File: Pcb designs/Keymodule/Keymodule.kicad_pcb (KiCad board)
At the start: 2 copper layers, 105 parts, among them J1 USB connect, U1 RP2040, U2 SN74LV1T34DBV, U3 AMS1117-3.3, U4 W25Q128JVS, Y1 ABM8-272-T3

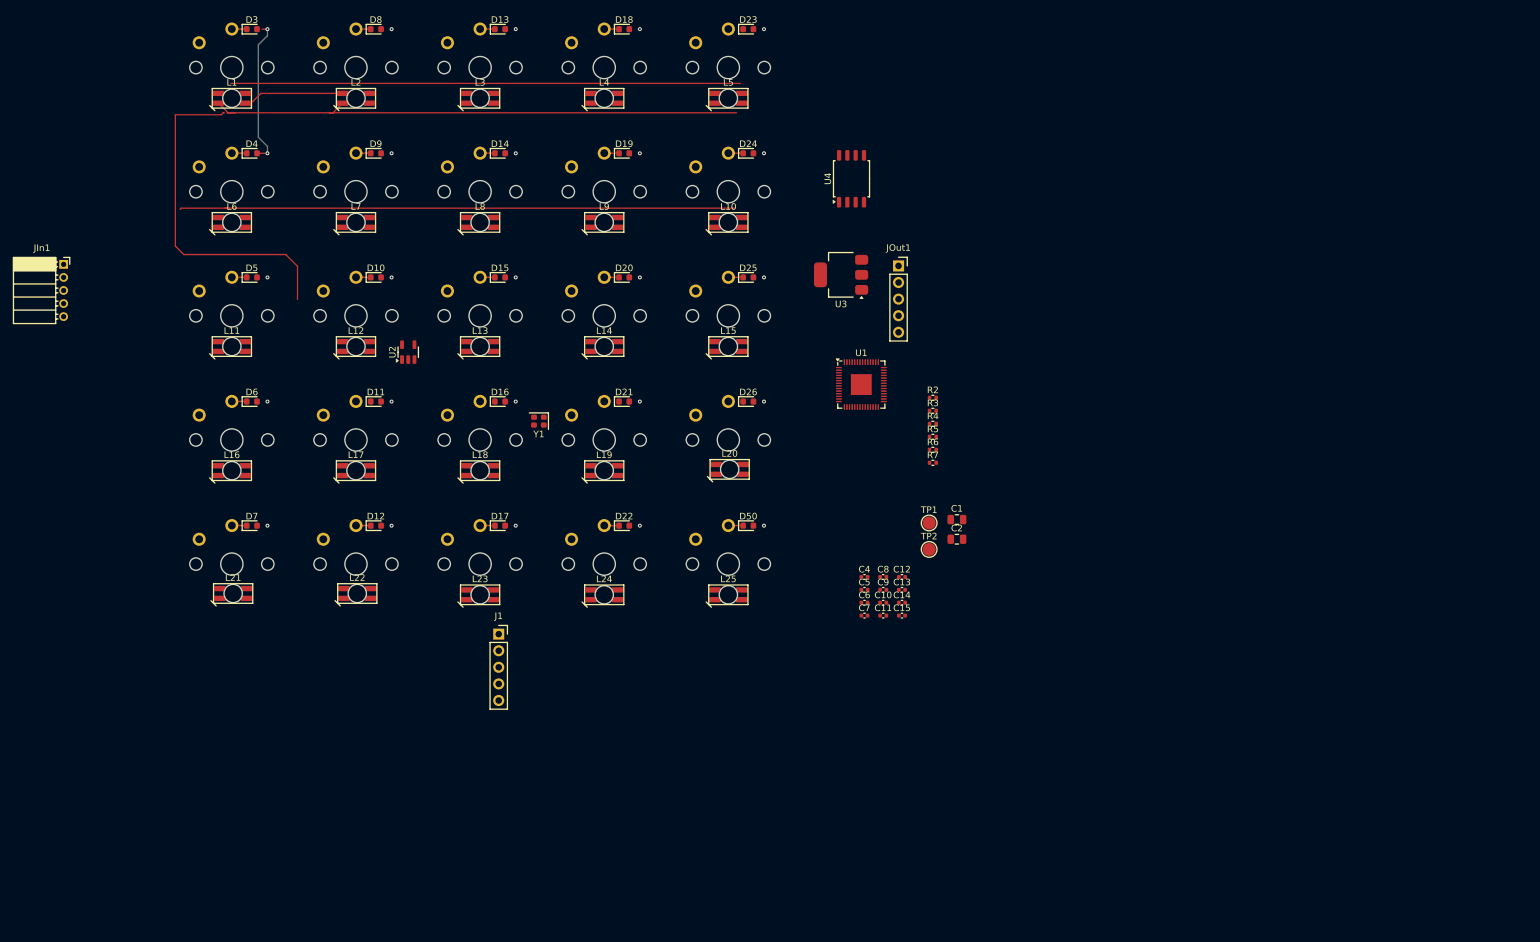
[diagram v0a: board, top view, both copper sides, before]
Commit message: Added traces to buttons
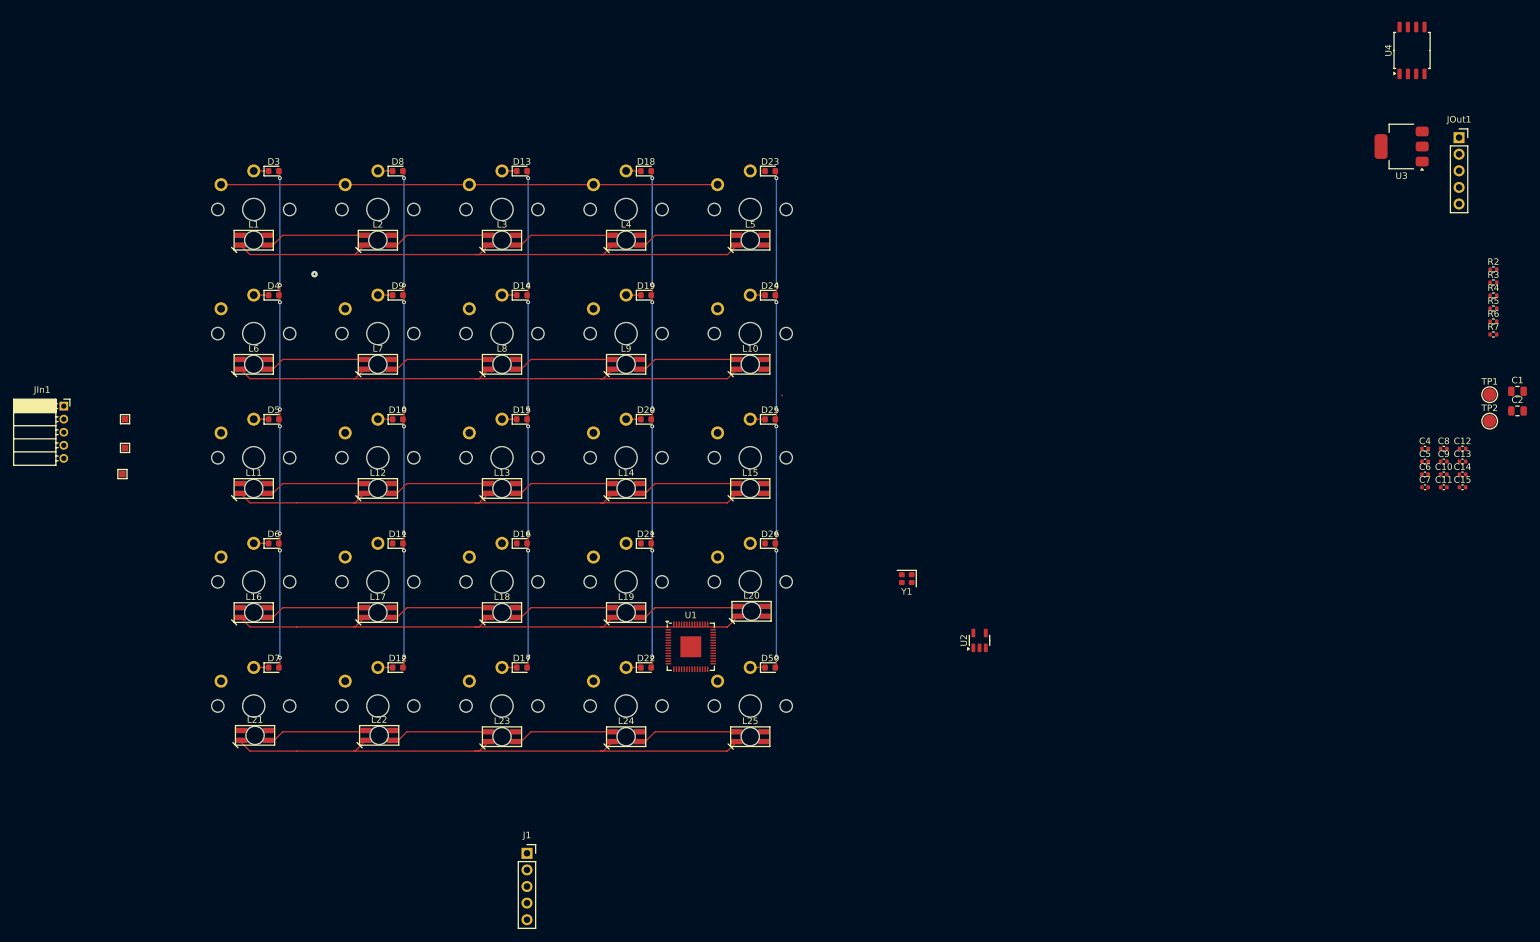
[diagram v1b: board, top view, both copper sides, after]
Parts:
- added REF**: TestPoint_Pad_1.0x1.0mm, TestPoint:TestPoint_Pad_1.0x1.0mm, F.Cu at (42.3, 94.1)
- added REF**: TestPoint_Pad_1.0x1.0mm, TestPoint:TestPoint_Pad_1.0x1.0mm, F.Cu at (41.9, 102.5)
- added REF**: TestPoint_Pad_1.0x1.0mm, TestPoint:TestPoint_Pad_1.0x1.0mm, F.Cu at (42.3, 98.5)
- moved U2 98.0 mm to (173.1, 128.0)
- moved C1 88.0 mm to (255.4, 89.8)
- moved C10 88.0 mm to (244.2, 102.6)
- moved C11 88.0 mm to (244.2, 104.5)
- moved C12 88.0 mm to (247.0, 98.6)
- moved C13 88.0 mm to (247.0, 100.6)
- moved C14 88.0 mm to (247.0, 102.6)
- moved C15 88.0 mm to (247.0, 104.5)
- moved C2 88.0 mm to (255.4, 92.8)
- moved C8 88.0 mm to (244.2, 98.6)
- moved C9 88.0 mm to (244.2, 100.6)
- moved JOut1 88.0 mm to (246.5, 51.0)
- moved TP1 88.0 mm to (251.2, 90.3)
- moved TP2 88.0 mm to (251.2, 94.4)
- moved U4 88.0 mm to (239.3, 37.7)
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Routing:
- net +5V: track 83.7 -> 422.9 mm
- net (no net): track 237.4 -> 0.14 mm, vias 25 -> 1
- net col0: track 0.00 -> 76.0 mm
- net row4: track 0.00 -> 75.3 mm, vias 0 -> 8
- net row3: track 0.00 -> 75.3 mm, vias 0 -> 8
- net row2: track 0.00 -> 75.3 mm, vias 0 -> 8
- net row1: track 0.00 -> 75.3 mm, vias 0 -> 8
- net row0: track 1.20 -> 75.6 mm, vias 0 -> 8
- net Net-(L4-DOUT): track 0.00 -> 15.5 mm
- net Net-(L24-DOUT): track 0.00 -> 15.5 mm
- net Net-(L19-DOUT): track 0.00 -> 15.5 mm
- net Net-(L14-DOUT): track 0.00 -> 15.5 mm
- net Net-(L10-DIN): track 0.00 -> 15.5 mm
- net Net-(L8-DOUT): track 0.00 -> 15.5 mm
- net Net-(L7-DOUT): track 0.00 -> 15.5 mm
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
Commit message: Stared wiring ic
LED signal boost not done
But its a start
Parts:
- added REF**: PinHeader_1x01_P1.27mm_Horizontal, Connector_PinHeader_1.27mm:PinHeader_1x01_P1.27mm_Horizontal, F.Cu at (139.9, 90.5)
- added REF**: PinHeader_1x01_P1.27mm_Horizontal, Connector_PinHeader_1.27mm:PinHeader_1x01_P1.27mm_Horizontal, F.Cu at (139.6, 109.5)
- added REF**: PinHeader_1x01_P1.27mm_Horizontal, Connector_PinHeader_1.27mm:PinHeader_1x01_P1.27mm_Horizontal, F.Cu at (60.5, 109.5)
- added REF**: PinHeader_1x01_P1.27mm_Horizontal, Connector_PinHeader_1.27mm:PinHeader_1x01_P1.27mm_Horizontal, F.Cu at (60.4, 90.5)
- added REF**: PinHeader_1x03_P1.27mm_Horizontal, Connector_PinHeader_1.27mm:PinHeader_1x03_P1.27mm_Horizontal, F.Cu at (50.9, 100.3)
- M_SW1, M_SW10, M_SW11, M_SW12, M_SW13, M_SW14, M_SW15, M_SW16, M_SW17, M_SW18, M_SW19, M_SW2, M_SW20, M_SW21, M_SW22, M_SW23, M_SW24, M_SW25, M_SW3, M_SW4, M_SW5, M_SW6, M_SW7, M_SW8, M_SW9: footprint 1_Custom_library:Kailh Switch 1350 -> 1_Custom_library:Kailh low profile Choc switch V1; moved to B.Cu
- moved C13 172.2 mm to (77.3, 71.7), turned to -90 degrees
- moved R5 169.7 mm to (82.1, 73.1), turned to 180 degrees
- moved C14 167.7 mm to (82.1, 72.0)
- moved U4 136.5 mm to (107.4, 72.6), turned to -90 degrees
- moved U2 132.0 mm to (56.0, 67.0), turned to -90 degrees
- moved R4 117.6 mm to (161.4, 150.4), turned to -90 degrees
- moved TP1 105.6 mm to (164.1, 150.0)
- moved C12 101.1 mm to (160.2, 150.4), turned to 90 degrees
- moved Y1 94.8 mm to (79.5, 71.7)
- moved C4 86.7 mm to (164.5, 138.9)
- moved C9 86.1 mm to (161.9, 126.2), turned to 90 degrees
- moved C10 82.5 mm to (174.2, 146.2)
- moved C11 82.5 mm to (174.2, 148.2)
- moved C15 82.5 mm to (177.1, 148.2)
- moved C5 82.5 mm to (171.3, 144.3)
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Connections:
- Y1 pad 4: GND -> unconnected-(Y1-Vdd-Pad4)
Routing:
- net GND: track 0.00 -> 694.7 mm
- net col4: track 0.00 -> 76.0 mm
- net col3: track 0.00 -> 76.0 mm
- net col2: track 0.00 -> 76.0 mm
- net +5V: track 422.9 -> 479.7 mm, vias 0 -> 2
- net col1: track 0.00 -> 38.0 mm
- net Net-(U1-GPIO15): track 0.00 -> 33.0 mm
- net row1: track 75.3 -> 44.2 mm, vias 8 -> 6
- net Net-(U1-QSPI_SD3): track 0.00 -> 20.4 mm
- net Net-(U1-QSPI_SCLK): track 0.00 -> 19.2 mm
- net col0: track 76.0 -> 57.0 mm
- net row2: track 75.3 -> 56.5 mm, vias 8 -> 6
- net Net-(U1-QSPI_SS): track 0.00 -> 18.3 mm
- net Net-(U1-QSPI_SD1): track 0.00 -> 17.1 mm
- net Net-(U1-QSPI_SD0): track 0.00 -> 16.8 mm
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
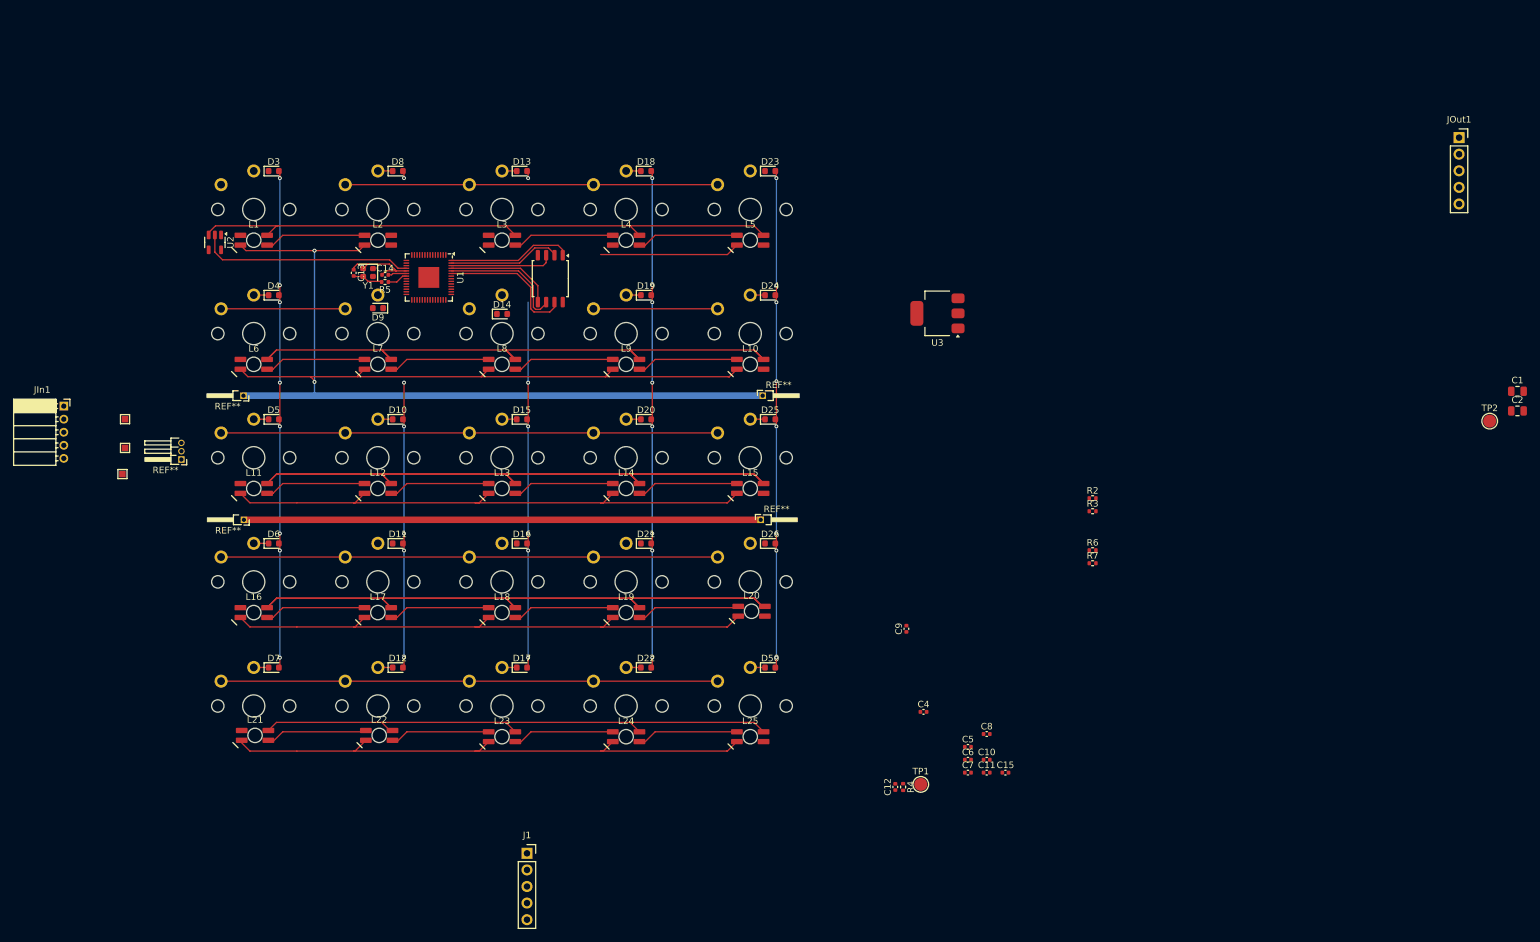
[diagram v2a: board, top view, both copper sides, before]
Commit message: Wired main power caps but to little space
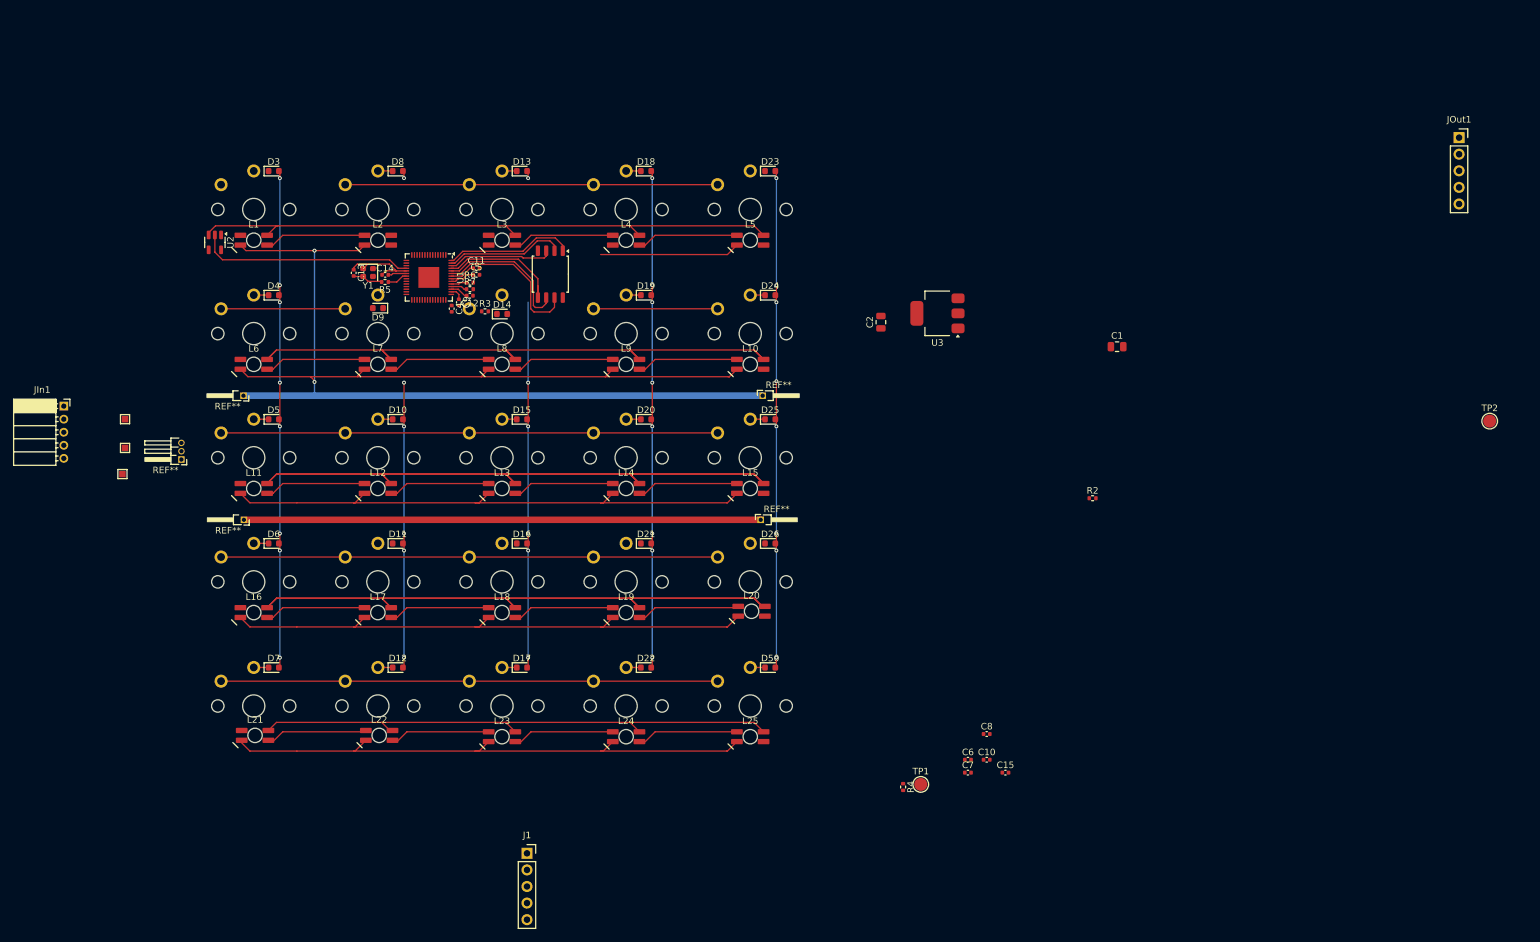
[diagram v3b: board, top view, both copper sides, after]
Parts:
- moved C11 109.8 mm to (96.1, 71.0)
- moved C5 104.3 mm to (96.1, 72.0)
- moved R7 104.1 mm to (95.1, 74.2)
- moved R6 103.7 mm to (95.1, 73.2)
- moved C12 99.5 mm to (95.1, 75.2), turned to 180 degrees
- moved C2 98.4 mm to (158.0, 79.2), turned to 90 degrees
- moved R3 97.9 mm to (97.4, 77.6)
- moved C4 95.0 mm to (92.3, 77.2), turned to -90 degrees
- moved C9 84.8 mm to (93.4, 76.2), turned to -90 degrees
- moved C1 61.7 mm to (194.2, 83.0)
- moved U4 0.69 mm to (107.4, 71.9)
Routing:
- net +1V1: track 0.00 -> 6.64 mm
- net Net-(U1-ADC_AVDD): track 0.00 -> 4.84 mm
- net Net-(U1-QSPI_SD3): track 20.4 -> 23.6 mm
- net Net-(U1-QSPI_SD0): track 16.8 -> 19.8 mm
- net USB_D-: track 0.00 -> 2.69 mm
- net USB_D+: track 0.00 -> 2.43 mm
- net Net-(U1-QSPI_SCLK): track 19.2 -> 21.4 mm
- net +3.3V: track 0.00 -> 2.07 mm
- net Net-(U1-QSPI_SS): track 18.3 -> 19.8 mm
- net Net-(U1-QSPI_SD1): track 17.1 -> 18.3 mm

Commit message: Getting there (4 layers)
Made the switch to a 4 layer PCB.
het is iets duurder maar wel de moeite waard.
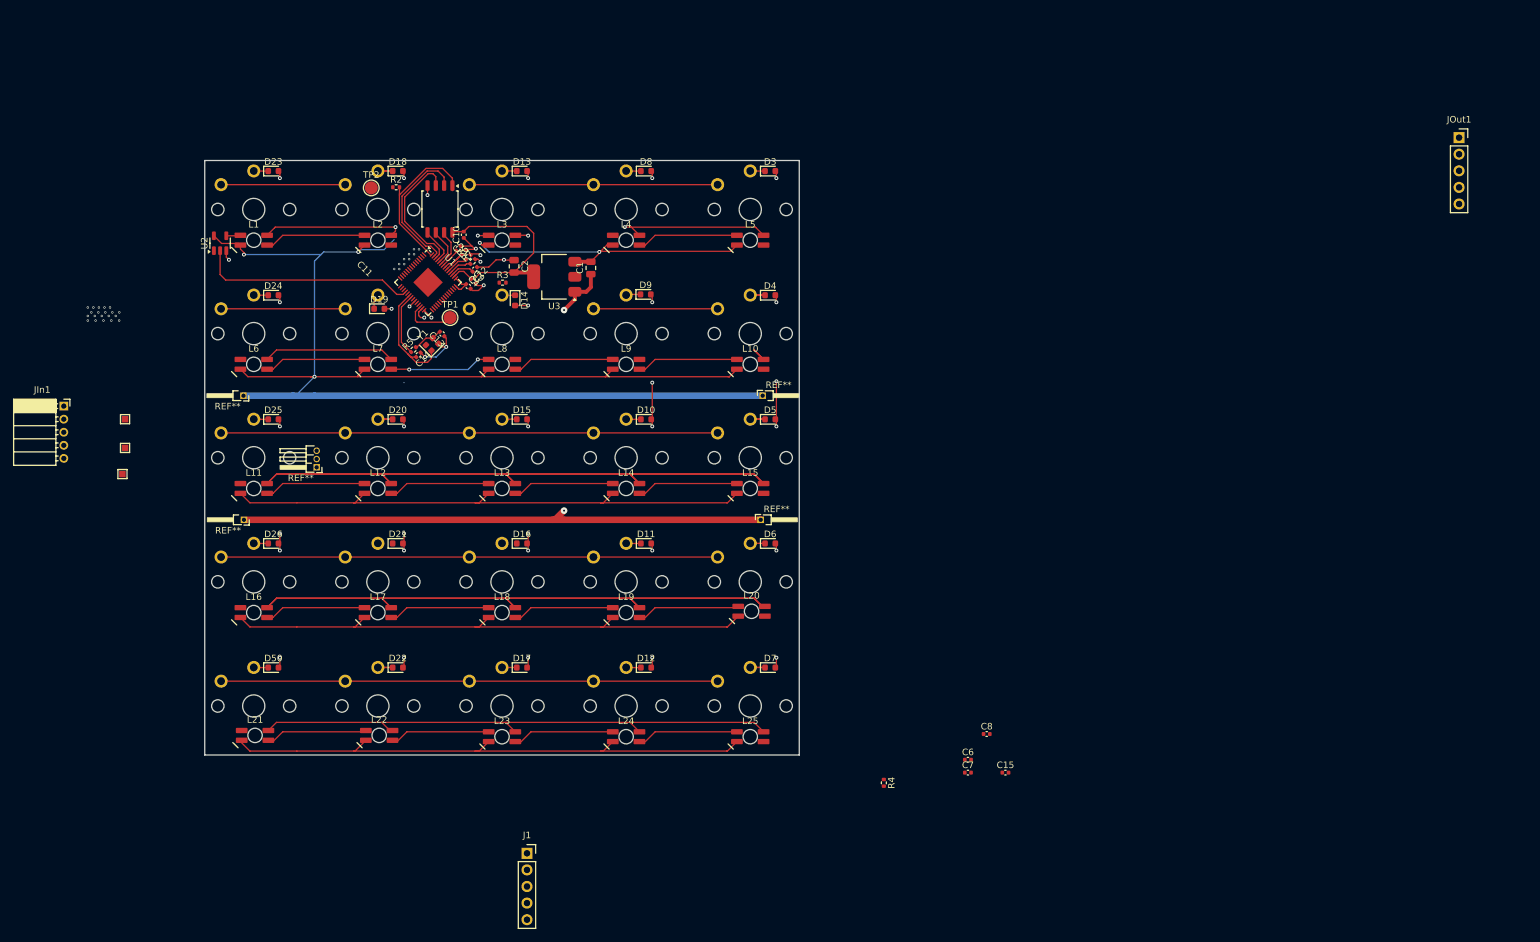
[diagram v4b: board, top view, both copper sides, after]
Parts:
- moved TP2 174.9 mm to (80.0, 58.7)
- moved R2 116.7 mm to (83.8, 58.6)
- moved C10 113.4 mm to (94.2, 65.9), turned to 90 degrees
- moved TP1 101.5 mm to (92.0, 78.5)
- moved C1 81.4 mm to (113.6, 71.0), turned to 90 degrees
- moved D23 76.1 mm to (65.0, 56.1)
- moved D24 76.1 mm to (65.0, 75.1)
- moved D25 76.1 mm to (65.0, 94.1)
- moved D26 76.1 mm to (65.0, 113.1)
- moved D50 76.1 mm to (65.0, 132.1)
- moved D3 76.0 mm to (141.1, 56.1)
- moved D4 76.0 mm to (141.1, 75.1)
- moved D5 76.0 mm to (141.1, 94.1)
- moved D6 76.0 mm to (141.1, 113.1)
- moved D7 76.0 mm to (141.1, 132.1)
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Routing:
- net +5V: track 479.7 -> 520.2 mm, vias 2 -> 5
- net row1: track 44.2 -> 78.4 mm
- net +3.3V: track 2.07 -> 34.5 mm
- net row2: track 56.5 -> 81.6 mm
- net Net-(U1-QSPI_SD3): track 23.6 -> 5.41 mm
- net GND: track 694.7 -> 710.6 mm, vias 0 -> 12
- net Net-(U1-QSPI_SCLK): track 21.4 -> 5.53 mm
- net Net-(L3-DOUT): track 14.6 -> 0.00 mm
- net Net-(U1-QSPI_SD0): track 19.8 -> 5.46 mm
- net Xin: track 2.99 -> 17.3 mm
- net Net-(U1-RUN): track 0.00 -> 8.16 mm
- net Xout: track 3.11 -> 9.75 mm
- net Net-(U1-ADC_AVDD): track 4.84 -> 10.5 mm
- net row3: track 75.3 -> 79.4 mm, vias 8 -> 6
- net Net-(U1-QSPI_SD2): track 16.1 -> 20.2 mm
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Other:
- board outline added: 91 x 91 mm
- copper layers 2 -> 4
- board text added: "Origin (Middle of PCB) X = 100 Y = 100"
